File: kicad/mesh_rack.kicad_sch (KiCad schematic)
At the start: 8 parts

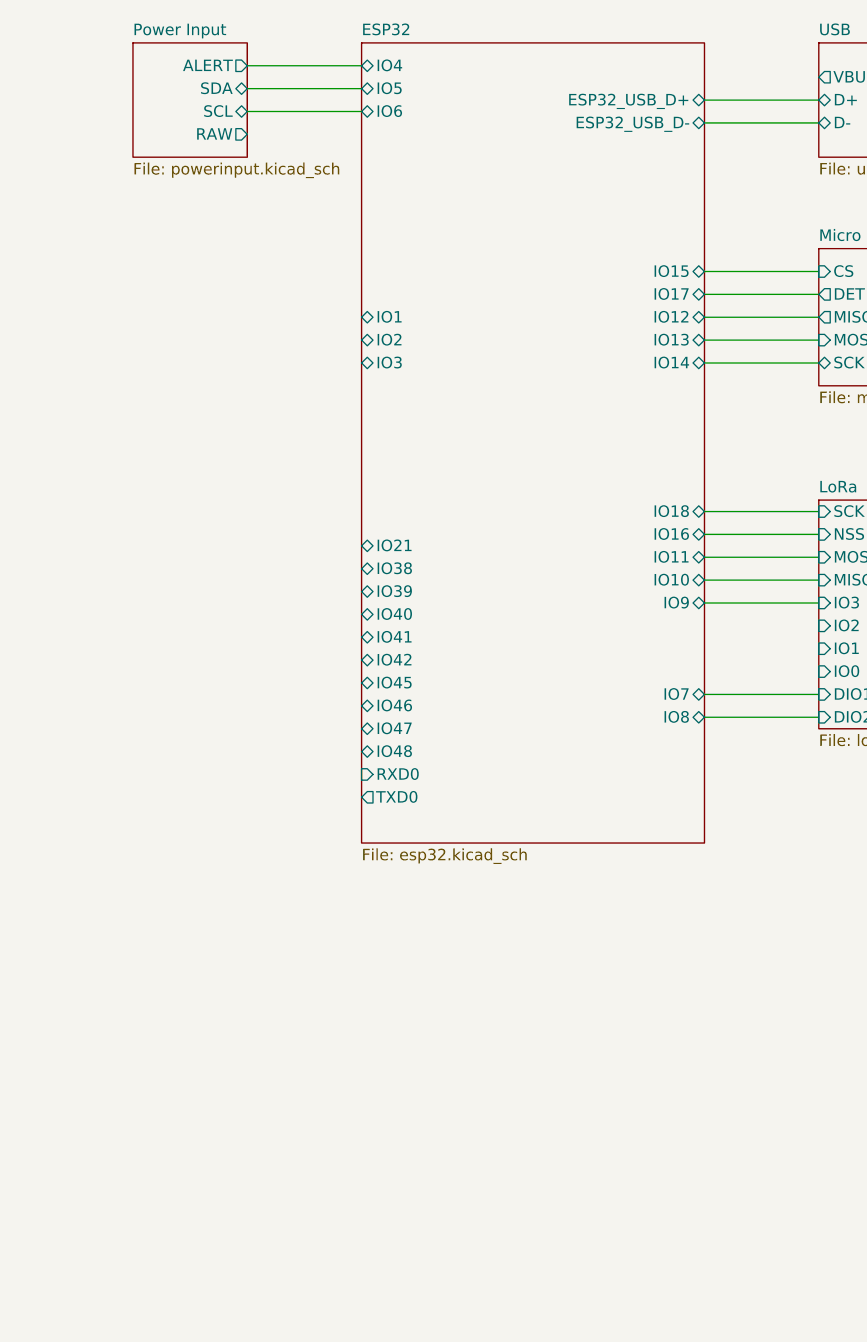
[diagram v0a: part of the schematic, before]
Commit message: add expansin headers
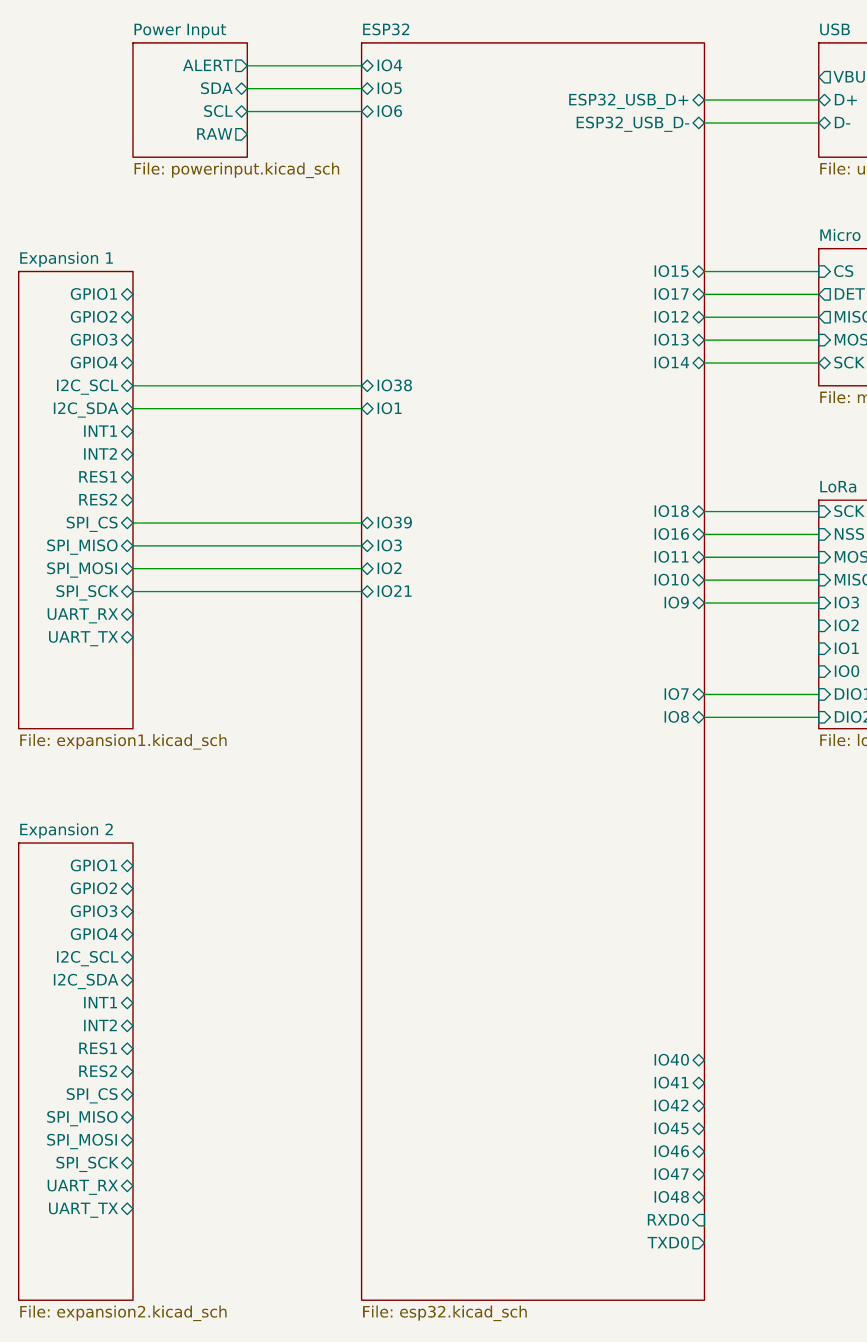
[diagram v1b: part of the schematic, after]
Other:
- added sheet Expansion 1 (expansion1.kicad_sch)
- added sheet Expansion 2 (expansion2.kicad_sch)

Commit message: finish pcb
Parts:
- added D4, D5, D6, D7, D8, D9: LED, LED_THT:LED_D5.0mm, symbol Device:LED
- added J10, J4: Conn_01x02, Connector_PinSocket_2.54mm:PinSocket_1x02_P2.54mm_Vertical, symbol Connector_Generic:Conn_01x02
- added R21, R22, R3, R5, R6, R7: 10k, Resistor_THT:R_Axial_DIN0207_L6.3mm_D2.5mm_P10.16mm_Horizontal, symbol Device:R_Small_US
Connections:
- net Power Input/RAW: now also D8.2 (A)
- new net: D7.1 (K), R7.1
- new net: D6.1 (K), R6.1
- new net: D8.1 (K), R21.1
- new net: D9.1 (K), R22.1
- new net: D5.1 (K), R5.1
- new net: D4.1 (K), R3.1
- new net ESP32/LED: D4.2 (A)
- new net ESP32/TST_PD0: D9.2 (A)
- new net GND: R21.2, R22.2, R3.2, R5.2, R6.2, R7.2
- new net GPS/GPS_SCL: J4.2 (Pin_2)
- new net GPS/GPS_SDA: J4.1 (Pin_1)
- new net GPS/GPS_USB_D+: J10.1 (Pin_1)
- new net GPS/GPS_USB_D-: J10.2 (Pin_2)
- new net GPS/TIMEPULSE: D5.2 (A)
- new net Power Input/3.3V: D6.2 (A)
- new net Power Input/5V: D7.2 (A)
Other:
- removed sheet Expansion 1
- removed sheet Expansion 2
- added sheet GPS (gps.kicad_sch)
- added sheet Headers (headers.kicad_sch)
- added sheet OLED (oled.kicad_sch)
- sheet ESP32 ports: added ADC1, LED, LORA_BUSY, LORA_DIO1, LORA_MISO, LORA_MOSI, LORA_NSS, LORA_RF_SW, LORA_RST, LORA_SCK, MCU_RXD0, MCU_TXD0, OLED_SCL, OLED_SDA, TST_PD0; removed IO1, IO10, IO18, IO21, IO38, IO39, IO40, IO41, IO42, IO48, IO8, IO9, RXD0, TXD0
- sheet LoRa ports: added BUSY, NRST, RXEN; removed DIO2, IO0, IO1, IO2, IO3
- sheet Power Input ports: added 3.3V, 5V; removed ALERT, SCL, SDA

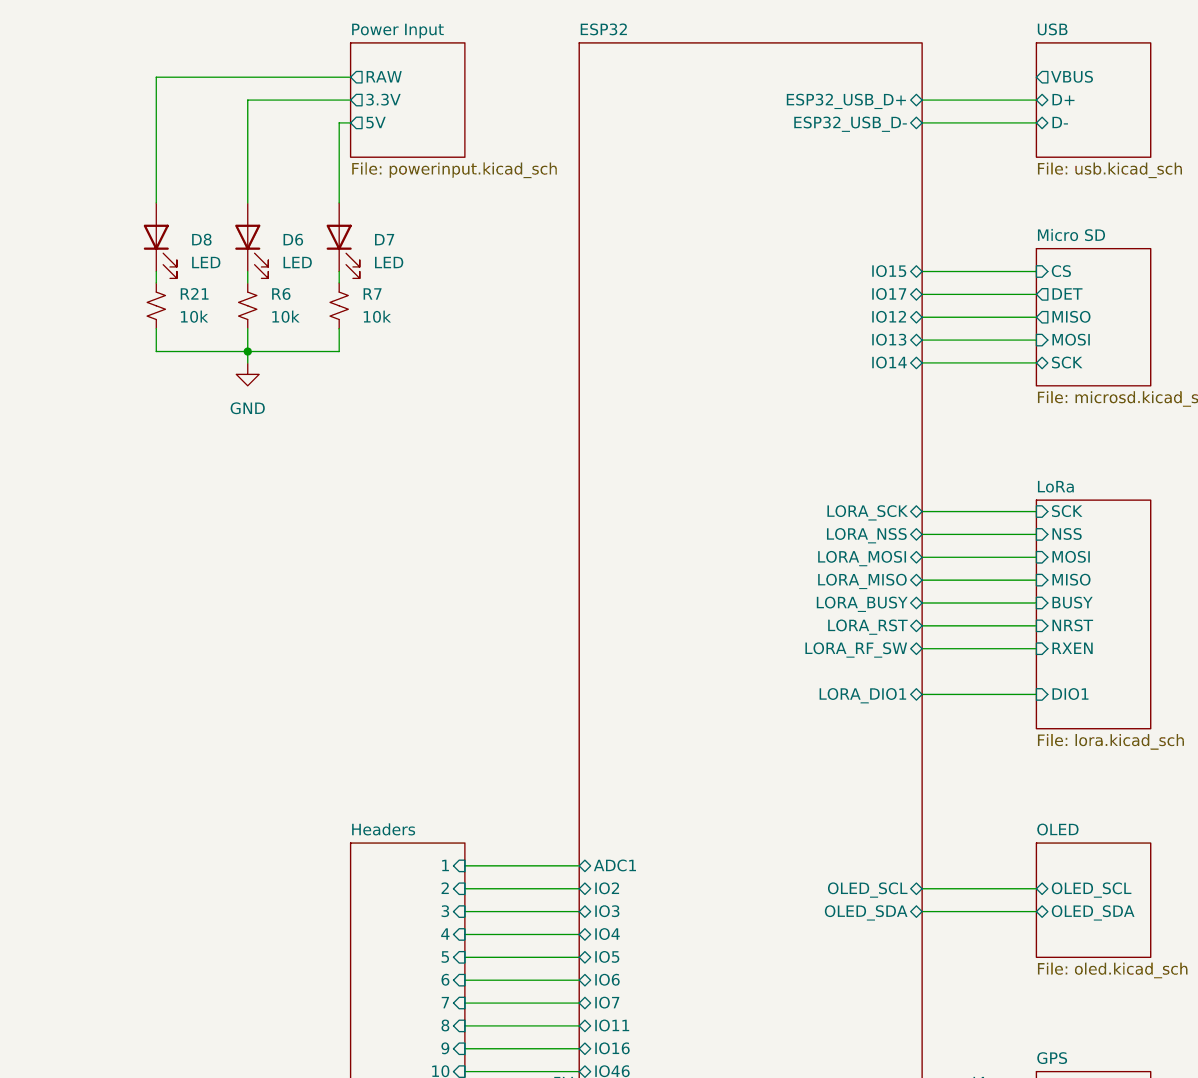
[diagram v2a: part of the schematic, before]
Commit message: add current sensor
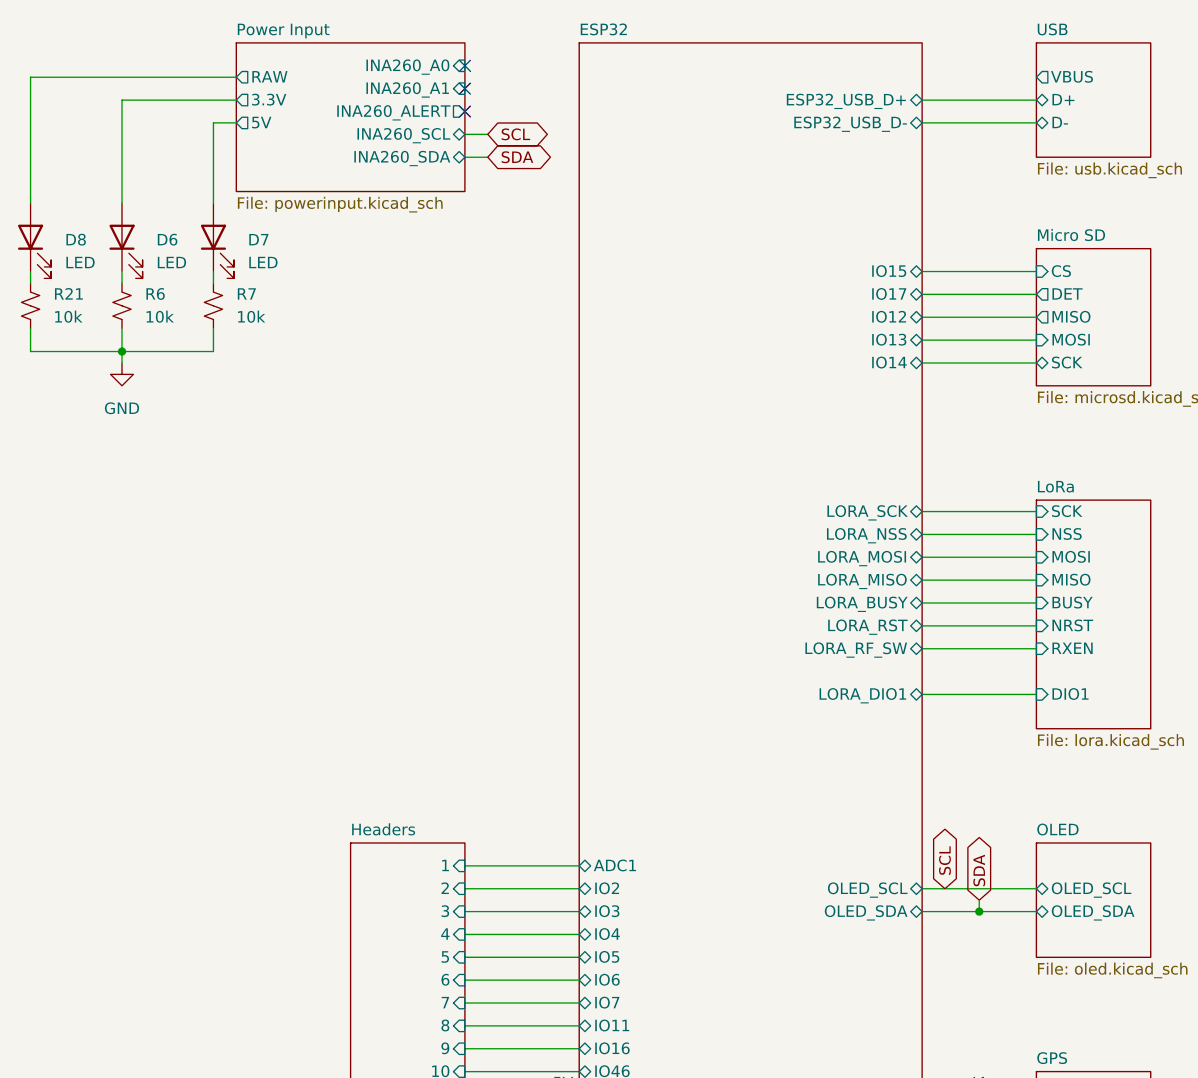
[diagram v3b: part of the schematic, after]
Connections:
- no-connect marks 0 -> 3
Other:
- sheet Power Input ports: added INA260_A0, INA260_A1, INA260_ALERT, INA260_SCL, INA260_SDA; removed none
- moved on the sheet: D6, D7, D8, R21, R6, R7

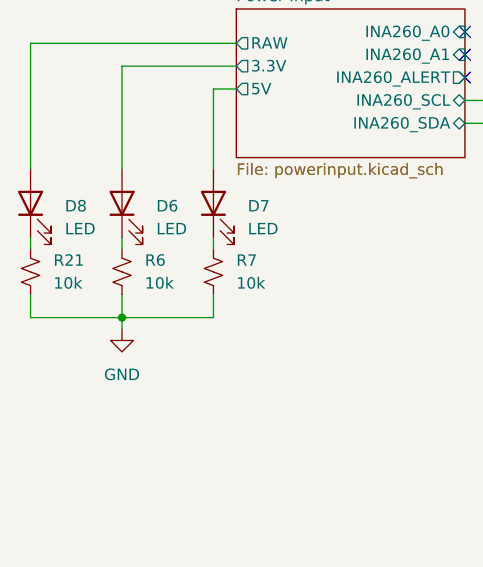
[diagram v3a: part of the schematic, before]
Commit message: make bom cheaper by using through hole parts
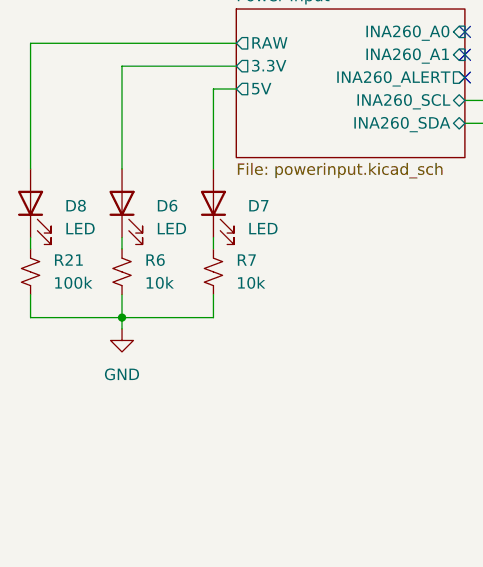
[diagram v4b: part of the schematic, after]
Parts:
- R21: value 10k -> 100k
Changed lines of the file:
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@@
 			)
 		)
-		(property "Value" "10k"
+		(property "Value" "100k"
 			(at 30.48 55.8799 0)
 			(effects

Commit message: make bom cheaper
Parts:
- R21, R22, R3, R5, R6, R7: footprint Resistor_THT:R_Axial_DIN0207_L6.3mm_D2.5mm_P10.16mm_Horizontal -> Resistor_THT:R_Axial_DIN0204_L3.6mm_D1.6mm_P2.54mm_Vertical
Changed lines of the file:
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@@
 			)
 		)
-		(property "Footprint" "Resistor_THT:R_Axial_DIN0207_L6.3mm_D2.5mm_P10.16mm_Horizontal"
+		(property "Footprint" "Resistor_THT:R_Axial_DIN0204_L3.6mm_D1.6mm_P2.54mm_Vertical"
 			(at 38.1 54.61 0)
 			(effects
@@
 			)
 		)
-		(property "Footprint" "Resistor_THT:R_Axial_DIN0207_L6.3mm_D2.5mm_P10.16mm_Horizontal"
+		(property "Footprint" "Resistor_THT:R_Axial_DIN0204_L3.6mm_D1.6mm_P2.54mm_Vertical"
 			(at 27.94 54.61 0)
 			(effects
@@
 			)
 		)
-		(property "Footprint" "Resistor_THT:R_Axial_DIN0207_L6.3mm_D2.5mm_P10.16mm_Horizontal"
+		(property "Footprint" "Resistor_THT:R_Axial_DIN0204_L3.6mm_D1.6mm_P2.54mm_Vertical"
 			(at 137.16 182.88 0)
 			(effects
@@
 			)
 		)
-		(property "Footprint" "Resistor_THT:R_Axial_DIN0207_L6.3mm_D2.5mm_P10.16mm_Horizontal"
+		(property "Footprint" "Resistor_THT:R_Axial_DIN0204_L3.6mm_D1.6mm_P2.54mm_Vertical"
 			(at 119.38 182.88 0)
 			(effects
@@
 			)
 		)
-		(property "Footprint" "Resistor_THT:R_Axial_DIN0207_L6.3mm_D2.5mm_P10.16mm_Horizontal"
+		(property "Footprint" "Resistor_THT:R_Axial_DIN0204_L3.6mm_D1.6mm_P2.54mm_Vertical"
 			(at 110.49 182.88 0)
 			(effects
@@
 			)
 		)
-		(property "Footprint" "Resistor_THT:R_Axial_DIN0207_L6.3mm_D2.5mm_P10.16mm_Horizontal"
+		(property "Footprint" "Resistor_THT:R_Axial_DIN0204_L3.6mm_D1.6mm_P2.54mm_Vertical"
 			(at 48.26 54.61 0)
 			(effects

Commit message: updadte
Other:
- added sheet Sensors (sensors.kicad_sch)
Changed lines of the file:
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@@
+	)
+	(sheet
+		(at 63.5 88.9)
+		(size 12.7 12.7)
+		(exclude_from_sim no)
+		(in_bom yes)
+		(on_board yes)
+		(dnp no)
+		(fields_autoplaced yes)
+		(stroke
+			(width 0.1524)
+			(type solid)
+		)
+		(fill
+			(color 255 255 194 1.0000)
+		)
+		(property "Sheetname" "Sensors"
+			(at 63.5 88.1884 0)
+			(effects
+				(font
+					(size 1.27 1.27)
+				)
+				(justify left bottom)
+			)
+		)
+		(property "Sheetfile" "sensors.kicad_sch"
+			(at 63.5 102.1846 0)
+			(effects
+				(font
+					(size 1.27 1.27)
+				)
+				(justify left top)
+			)
+		)
+		(instances
+			(project "mesh_rack"
+				(path "/78341cab-a048-4351-a366-4c432cce3019"
+					(page "10")
+				)
+			)
+		)
 	)
 	(sheet
